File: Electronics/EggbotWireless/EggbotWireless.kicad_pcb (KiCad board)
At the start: 2 copper layers, 118 x 40 mm, 90 parts, among them J1 BATT, J2 Conn_01x03_Male, J3 USB_B_Micro, J4 AVR-ISP-6, J5 Conn_01x03_Female, J6 Conn_01x05_Male, M1 , M2 , M3 Motor_Servo, Q1 FDD8800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

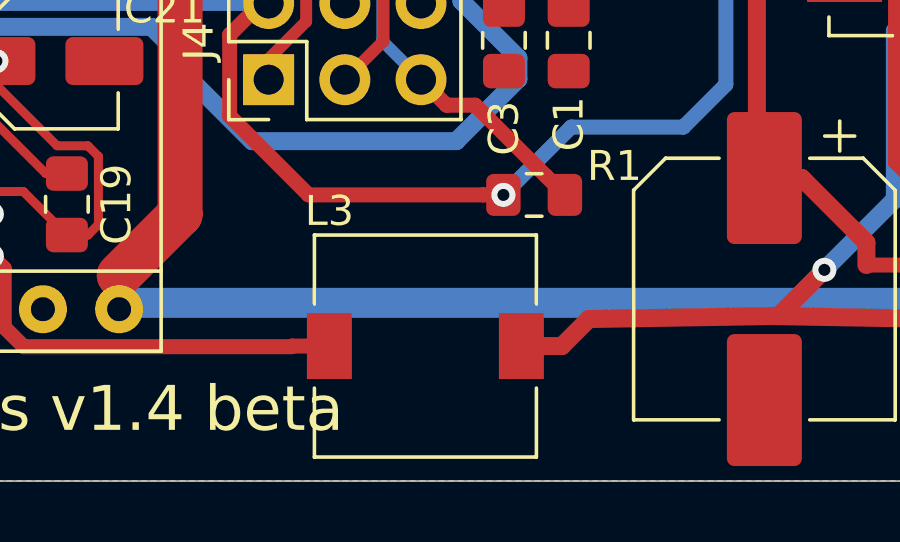
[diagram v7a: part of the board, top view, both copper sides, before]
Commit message: change 5vboost inductor to smaller
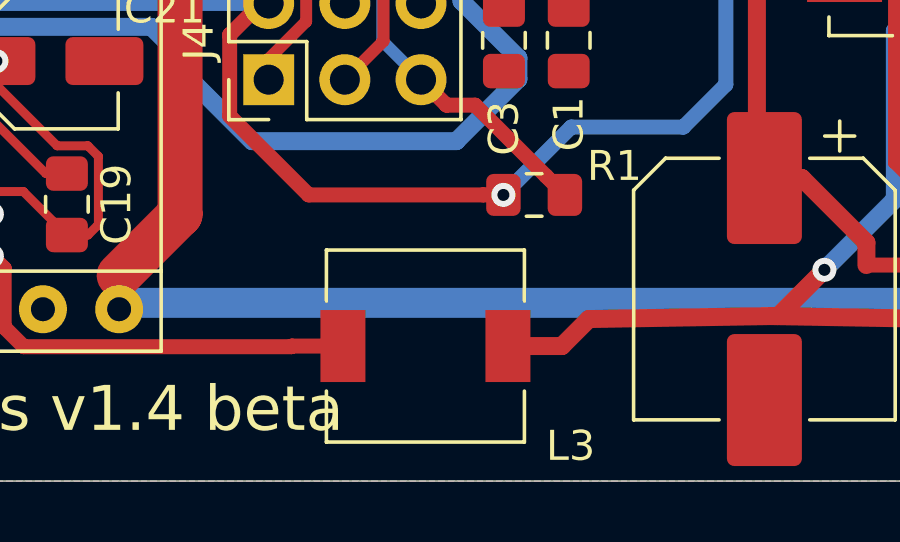
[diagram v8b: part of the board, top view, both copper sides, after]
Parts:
- L3: footprint Inductor_SMD:L_7.3x7.3_H4.5 -> Inductor_SMD:L_6.3x6.3_H3
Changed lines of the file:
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@@
     (add_net +12V)
+  )
+  (module Inductor_SMD:L_6.3x6.3_H3 (layer F.Cu)
+    (at 59.564 73.028 180)
+    (descr "Choke, SMD, 6.3x6.3mm 3mm height")
+    (tags "Choke SMD")
+    (attr smd)
+    (fp_text reference L3 (at -4.84 -3.33) (layer F.SilkS)
+      (effects (font (size 1 1) (thickness 0.15)))
+    )
+    (fp_text value 6.8uH (at 0 4.45) (layer F.Fab)
+      (effects (font (size 1 1) (thickness 0.15)))
+    )
+    (fp_arc (start 0 0) (end 1.91 1.91) (angle 90) (layer F.Fab) (width 0.1))
+    (fp_arc (start 0 0) (end -1.91 -1.91) (angle 90) (layer F.Fab) (width 0.1))
+    (fp_line (start -3.15 3.15) (end 3.15 3.15) (layer F.Fab) (width 0.1))
+    (fp_line (start -3.15 -3.15) (end 3.15 -3.15) (layer F.Fab) (width 0.1))
+    (fp_line (start -3.15 -3.15) (end -3.15 -1.5) (layer F.Fab) (width 0.1))
+    (fp_line (start -3.15 3.15) (end -3.15 1.5) (layer F.Fab) (width 0.1))
+    (fp_line (start 3.15 -3.15) (end 3.15 -1.5) (layer F.Fab) (width 0.1))
+    (fp_line (start 3.15 3.15) (end 3.15 1.5) (layer F.Fab) (width 0.1))
+    (fp_line (start 3.75 -3.4) (end -3.75 -3.4) (layer F.CrtYd) (width 0.05))
+    (fp_line (start 3.75 3.4) (end 3.75 -3.4) (layer F.CrtYd) (width 0.05))
+    (fp_line (start -3.75 3.4) (end 3.75 3.4) (layer F.CrtYd) (width 0.05))
+    (fp_line (start -3.75 -3.4) (end -3.75 3.4) (layer F.CrtYd) (width 0.05))
+    (fp_line (start 3.3 -3.2) (end 3.3 -1.5) (layer F.SilkS) (width 0.12))
+    (fp_line (start -3.3 -3.2) (end 3.3 -3.2) (layer F.SilkS) (width 0.12))
+    (fp_line (start -3.3 -1.5) (end -3.3 -3.2) (layer F.SilkS) (width 0.12))
+    (fp_line (start -3.3 3.2) (end -3.3 1.5) (layer F.SilkS) (width 0.12))
+    (fp_line (start 3.3 3.2) (end -3.3 3.2) (layer F.SilkS) (width 0.12))
+    (fp_line (start 3.3 1.5) (end 3.3 3.2) (layer F.SilkS) (width 0.12))
+    (fp_text user %R (at 0 0) (layer F.Fab)
+      (effects (font (size 1 1) (thickness 0.15)))
+    )
+    (pad 2 smd rect (at 2.75 0 180) (size 1.5 2.4) (layers F.Cu F.Paste F.Mask)
+      (net 75 "Net-(D5-Pad2)"))
+    (pad 1 smd rect (at -2.75 0 180) (size 1.5 2.4) (layers F.Cu F.Paste F.Mask)
+      (net 58 +5V))
+    (model ${KISYS3DMOD}/Inductor_SMD.3dshapes/L_6.3x6.3_H3.wrl
+      (at (xyz 0 0 0))
+      (scale (xyz 1 1 1))
+      (rotate (xyz 0 0 0))
+    )
   )
   (module Module:Pololu_Breakout-16_15.2x20.3mm (layer F.Cu)
@@
       (at (xyz 0 0 0))
       (scale (xyz 1 1 1))
-      (rotate (xyz 0 0 0))
-    )
-  )
-  (module Inductor_SMD:L_7.3x7.3_H4.5 (layer F.Cu)
-    (at 59.564 73.028 180)
-    (descr "Choke, SMD, 7.3x7.3mm 4.5mm height")
-    (tags "Choke SMD")
-    (attr smd)
-    (fp_text reference L3 (at 3.2 4.5) (layer F.SilkS)
-      (effects (font (size 1 1) (thickness 0.15)))
-    )
-    (fp_text value 6.8uH (at 0 4.45) (layer F.Fab)
-      (effects (font (size 1 1) (thickness 0.15)))
-    )
-    (fp_arc (start 0 0) (end -2.29 -2.29) (angle 90) (layer F.Fab) (width 0.1))
-    (fp_arc (start 0 0) (end 2.29 2.29) (angle 90) (layer F.Fab) (width 0.1))
-    (fp_line (start -3.65 -3.65) (end 3.65 -3.65) (layer F.Fab) (width 0.1))
-    (fp_line (start 3.65 3.65) (end -3.65 3.65) (layer F.Fab) (width 0.1))
-    (fp_line (start -3.65 -3.65) (end -3.65 -1.4) (layer F.Fab) (width 0.1))
-    (fp_line (start -3.65 3.65) (end -3.65 1.4) (layer F.Fab) (width 0.1))
-    (fp_line (start 3.65 -3.65) (end 3.65 -1.4) (layer F.Fab) (width 0.1))
-    (fp_line (start 3.65 3.65) (end 3.65 1.4) (layer F.Fab) (width 0.1))
-    (fp_line (start 4.2 -3.9) (end -4.2 -3.9) (layer F.CrtYd) (width 0.05))
-    (fp_line (start 4.2 3.9) (end 4.2 -3.9) (layer F.CrtYd) (width 0.05))
-    (fp_line (start -4.2 3.9) (end 4.2 3.9) (layer F.CrtYd) (width 0.05))
-    (fp_line (start -4.2 -3.9) (end -4.2 3.9) (layer F.CrtYd) (width 0.05))
-    (fp_line (start 3.7 -3.7) (end 3.7 -1.4) (layer F.SilkS) (width 0.12))
-    (fp_line (start -3.7 -3.7) (end 3.7 -3.7) (layer F.SilkS) (width 0.12))
-    (fp_line (start -3.7 -1.4) (end -3.7 -3.7) (layer F.SilkS) (width 0.12))
-    (fp_line (start -3.7 3.7) (end -3.7 1.4) (layer F.SilkS) (width 0.12))
-    (fp_line (start 3.7 3.7) (end -3.7 3.7) (layer F.SilkS) (width 0.12))
-    (fp_line (start 3.7 1.4) (end 3.7 3.7) (layer F.SilkS) (width 0.12))
-    (fp_text user %R (at 0 0) (layer F.Fab)
-      (effects (font (size 1 1) (thickness 0.15)))
-    )
-    (pad 2 smd rect (at 3.2 0 180) (size 1.5 2.2) (layers F.Cu F.Paste F.Mask)
-      (net 75 "Net-(D5-Pad2)"))
-    (pad 1 smd rect (at -3.2 0 180) (size 1.5 2.2) (layers F.Cu F.Paste F.Mask)
-      (net 58 +5V))
-    (model ${KISYS3DMOD}/Inductor_SMD.3dshapes/L_7.3x7.3_H4.5.wrl
-      (at (xyz 0 0 0))
-      (scale (xyz 1 1 1))
